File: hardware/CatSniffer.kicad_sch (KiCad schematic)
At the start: 91 parts, among them J1 Antenna, J2 Conn_01x06_Female, J3 Conn_01x06_Female, P1 USB_C_Plug_USB2.0, SW1 SW, U1 AP2112K-3.3, U2 RFSW8006QTR7, U3 RP2040, U4 0900PC15A0036, U5 0900FM15D0039, U6 PE42421, U7 SX1262IMLTRT, U8 CC1352P1F3RGZT, U9 W25Q16JV, Y1 48MHz, Y2 32.768kHz, Y3 32Mhz, Y4 12MHz

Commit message: routing rp2040
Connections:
- net +3V3: no longer J2.1 (Pin_1)
- net GND: no longer J2.5 (Pin_5)
- net LED1: now also U3.40 (GPIO28_ADC2); no longer U3.27 (GPIO16)
- net LED2: now also U3.39 (GPIO27_ADC1); no longer U3.28 (GPIO17)
- net RESET: no longer J2.3 (Pin_3)
- net SWCLK: no longer J2.4 (Pin_4)
- net SWDIO: no longer J2.2 (Pin_2)
- net U_SWITCH: no longer names the net of U3.34 (GPIO22)
- no-connect marks 30 -> 36

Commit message: Change footprint
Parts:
- U2: footprint Package_DFN_QFN:DFN-8-1EP_2x2mm_P0.5mm_EP0.9x1.3mm -> CatSniffer:SON50P200X200X90-9N
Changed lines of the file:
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@@
     (property "Reference" "U2" (id 0) (at 533.019 60.833 0))
     (property "Value" "RFSW8006QTR7" (id 1) (at 533.019 63.1444 0))
-    (property "Footprint" "Package_DFN_QFN:DFN-8-1EP_2x2mm_P0.5mm_EP0.9x1.3mm" (id 2) (at 532.384 62.484 0)
+    (property "Footprint" "CatSniffer:SON50P200X200X90-9N" (id 2) (at 532.384 62.484 0)
       (effects (font (size 1.27 1.27)) hide)
     )
@@
     )
     (path "/00000000-0000-0000-0000-0000609fac26"
-      (reference "U2") (unit 1) (value "RFSW8006QTR7") (footprint "Package_DFN_QFN:DFN-8-1EP_2x2mm_P0.5mm_EP0.9x1.3mm")
+      (reference "U2") (unit 1) (value "RFSW8006QTR7") (footprint "CatSniffer:SON50P200X200X90-9N")
     )
     (path "/aa0ffc82-ac04-4d0c-acef-b136b502cce4"

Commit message: update_bom
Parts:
- C3, C38: Mouser# 963-MAASA105CD7105MF -> 963-MSRLJ103SB5105MF; manf# MAASA105CD7105MFCA01 -> MSRLJ103SB5105MFNA01
- Y4: LCSC# C521581 -> C2848217; manf# XXHBBCNANF-12.000000MHZ -> XC32M4-12.000-F20NJDT
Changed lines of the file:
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@@
       (effects (font (size 1.27 1.27)) hide)
     )
-    (property "manf#" "MAASA105CD7105MFCA01" (id 5) (at 283.21 130.81 0)
+    (property "manf#" "MSRLJ103SB5105MFNA01" (id 5) (at 283.21 130.81 0)
       (effects (font (size 1.27 1.27)) hide)
     )
@@
       (effects (font (size 1.27 1.27)) hide)
     )
-    (property "Mouser#" "963-MAASA105CD7105MF" (id 7) (at 283.21 130.81 0)
+    (property "Mouser#" "963-MSRLJ103SB5105MF" (id 7) (at 283.21 130.81 0)
       (effects (font (size 1.27 1.27)) hide)
     )
@@
       (effects (font (size 1.27 1.27)) hide)
     )
-    (property "manf#" "MAASA105CD7105MFCA01" (id 5) (at 321.31 130.81 0)
+    (property "manf#" "MSRLJ103SB5105MFNA01" (id 5) (at 321.31 130.81 0)
       (effects (font (size 1.27 1.27)) hide)
     )
@@
       (effects (font (size 1.27 1.27)) hide)
     )
-    (property "Mouser#" "963-MAASA105CD7105MF" (id 7) (at 321.31 130.81 0)
+    (property "Mouser#" "963-MSRLJ103SB5105MF" (id 7) (at 321.31 130.81 0)
       (effects (font (size 1.27 1.27)) hide)
     )
@@
       (effects (font (size 1.27 1.27)) hide)
     )
-    (property "LCSC#" "C521581" (id 4) (at 290.83 86.36 0)
-      (effects (font (size 1.27 1.27)) hide)
-    )
-    (property "manf#" "XXHBBCNANF-12.000000MHZ" (id 5) (at 290.83 86.36 0)
-      (effects (font (size 1.27 1.27)) hide)
-    )
+    (property "LCSC#" "C2848217" (id 4) (at 290.83 86.36 0)
+      (effects (font (size 1.27 1.27)) hide)
+    )
+    (property "manf#" "XC32M4-12.000-F20NJDT" (id 5) (at 290.83 86.36 0)
+      (effects (font (size 1.27 1.27)) hide)
+    )

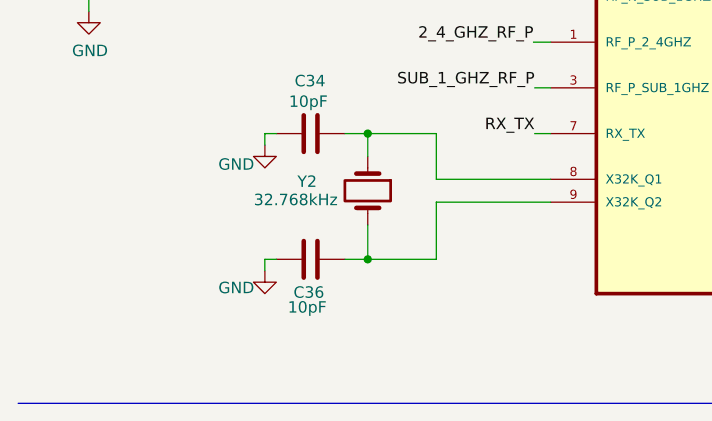
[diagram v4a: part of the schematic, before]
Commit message: fix BOM and add 3d components
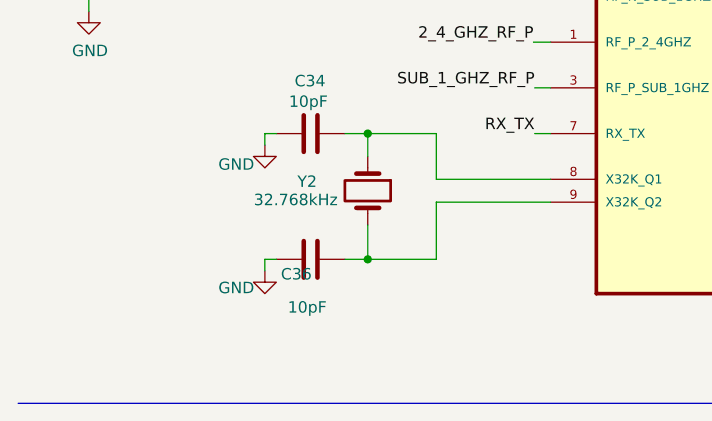
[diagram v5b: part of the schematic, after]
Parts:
- P1: LCSC# C393939 -> C709357; manf# TYPE-C16PIN -> KH-TYPE-C-16P
- U8: Mouser# (none) -> 595-CC1352P1F3RGZT; manf# (none) -> CC1352P1F3RGZT; provedor (none) -> Mouser

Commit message: fix SPI RF port
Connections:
- net CIPO: now also U3.27 (GPIO16); no longer U3.11 (GPIO8)
- net COPI: now also U3.30 (GPIO19); no longer U3.9 (GPIO7)
- net CTF1: now also U3.11 (GPIO8); no longer U3.30 (GPIO19)
- net CTF2: now also U3.12 (GPIO9); no longer U3.29 (GPIO18)
- net NSS: now also U3.28 (GPIO17); no longer U3.12 (GPIO9)
- net SCK: now also U3.29 (GPIO18); no longer U3.8 (GPIO6)

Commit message: add components replacements and fix "antena" serigraphy
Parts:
- C10, C11, C12, C13, C15, C16, C32: Remplazos (none) -> C162178
- C25, C26: Remplazos (none) -> C1660
- C34, C36: Remplazos (none) -> C91367
- L4: Remplazos (none) -> C90210
- L5: Remplazos (none) -> C2885870
- R1, R2: Remplazos (none) -> C311919
- R3, R4, R5, R9: Remplazos (none) -> C705847
- R6: Remplazos (none) -> C25803
- U8: Availability In Stock -> (none); MF Texas Instruments -> (none); MP CC1352P1F3RGZT -> (none); Package VQFN-48 Texas Instruments -> (none); Price None -> (none); Purchase-URL https://pricing.snapeda.com/search/part/CC1352P1F3RGZT/?ref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 -> (none)

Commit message: update RF switch connected to microcontroller
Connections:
- net DIO2: now also JP1.3 (B); no longer JP1.1 (A)
- net DIO22: now also JP1.1 (A); no longer JP1.3 (B)
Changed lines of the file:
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@@
     )
   )
-  (symbol (lib_id "CatSniffer-rescue:Jumper_3_Bridged12-Jumper-CatStick-rescue-CatSniffer-rescue") (at 551.561 200.406 0) (mirror y) (unit 1)
+  (symbol (lib_id "CatSniffer-rescue:Jumper_3_Bridged12-Jumper-CatStick-rescue-CatSniffer-rescue") (at 551.561 200.406 0) (unit 1)
     (in_bom yes) (on_board yes) (dnp no)
     (property "Reference" "JP1" (at 551.561 195.2244 0)
